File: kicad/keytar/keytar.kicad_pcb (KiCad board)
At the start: 2 copper layers, 9 parts, among them J1 DIN-5_180degree, J2 USB_B, J3 Conn_01x02, U1 Pico

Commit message: properly implement PCB
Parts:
- added  : MountingHole_3.2mm_M3, MountingHole:MountingHole_3.2mm_M3, F.Cu at (59.0, -7.02)
- added  : MountingHole_3.2mm_M3, MountingHole:MountingHole_3.2mm_M3, F.Cu at (19.2, -58.0)
- added J4: Conn_01x04, Connector_PinHeader_2.54mm:PinHeader_1x04_P2.54mm_Horizontal, F.Cu at (21.4, -38.6)
- J1: value DIN-5_180degree -> (none)
- R1, R2, R3: footprint Resistor_THT:R_Axial_DIN0411_L9.9mm_D3.6mm_P5.08mm_Vertical -> Resistor_THT:R_Axial_DIN0411_L9.9mm_D3.6mm_P12.70mm_Horizontal
- moved J3 189.7 mm to (8.94, -38.6), turned to 270 degrees
- moved R3 187.2 mm to (4.75, -47.9), turned to 0 degrees
- moved R1 159.7 mm to (52.7, -70.1), turned to 270 degrees
- moved U1 157.6 mm to (38.0, -46.2)
- moved RV1 144.8 mm to (52.5, -76.5), turned to 0 degrees
- moved RV2 144.4 mm to (8.51, -76.5), turned to 0 degrees
- moved J1 140.6 mm to (64.4, -61.0), turned to 90 degrees
- moved R2 134.0 mm to (52.7, -53.4), turned to 270 degrees
- moved J2 100.1 mm to (60.9, -42.6), turned to 0 degrees
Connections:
- J1 pad 2: Net-(J1-Pad2) -> GND
- U1 pad 3: Net-(J1-Pad2) -> GND
- U1 pad 38: GND -> Net-(U1-Pad38)
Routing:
- net Net-(J3-Pad2): track 20.4 -> 126.8 mm
- net Net-(J4-Pad2): track 0.00 -> 63.9 mm
- net Net-(RV2-Pad2): track 0.00 -> 58.6 mm
- net GND: track 0.00 -> 53.2 mm
- net Net-(R2-Pad2): track 0.00 -> 43.3 mm
- net Net-(J2-Pad1): track 0.00 -> 33.5 mm
- net Net-(RV1-Pad2): track 0.00 -> 33.0 mm
- net Net-(J3-Pad1): track 20.3 -> 46.3 mm
- net Net-(J4-Pad4): track 0.00 -> 17.9 mm
- net Net-(R3-Pad1): track 100.1 -> 114.9 mm
- net Net-(J4-Pad3): track 0.00 -> 14.3 mm
- net Net-(J2-Pad5): track 0.00 -> 12.0 mm
- net Net-(J4-Pad1): track 0.00 -> 8.33 mm
- net Net-(J1-Pad5): track 9.78 -> 7.25 mm
- net Net-(J1-Pad4): track 9.78 -> 7.93 mm
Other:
- board outline added: 76 x 95 mm
- board text added: "Garbage Keytar v0.1 designed by AberDerBart"

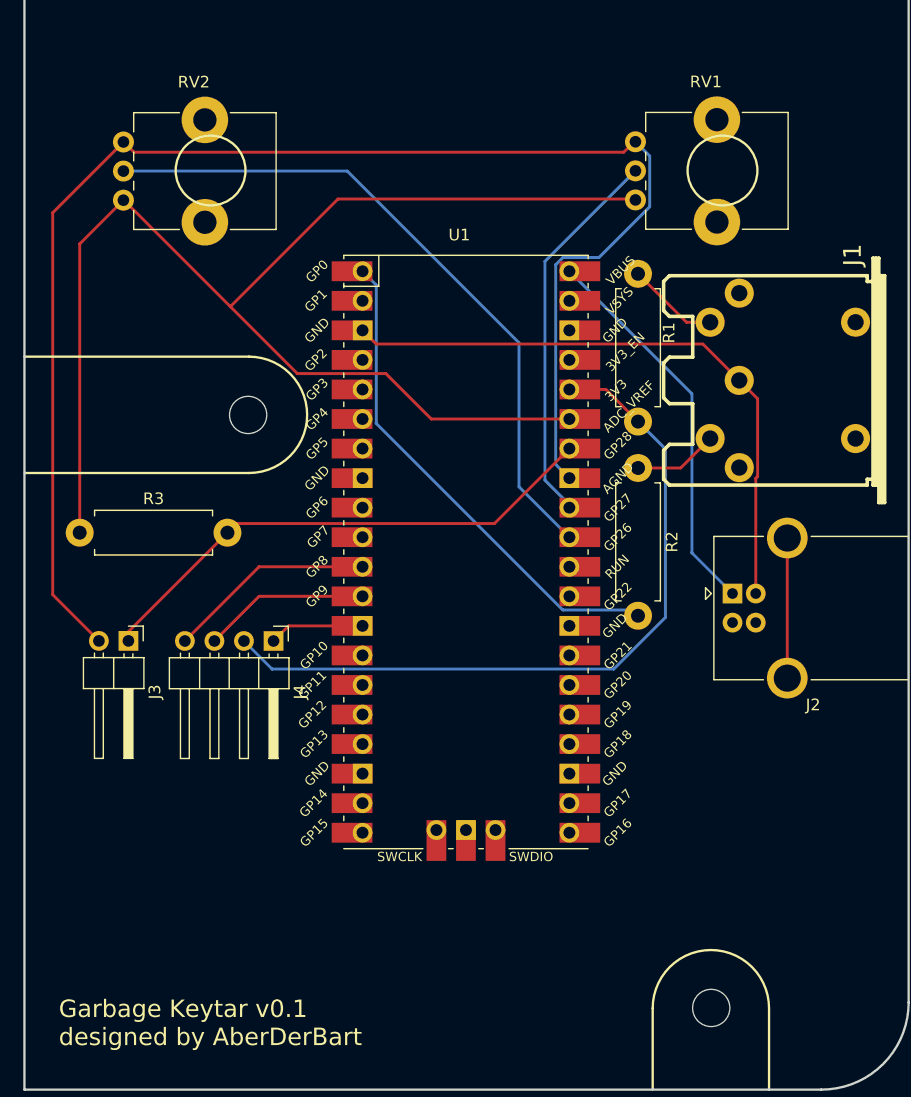
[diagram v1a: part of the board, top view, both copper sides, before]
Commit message: add power via MIDI to pcb
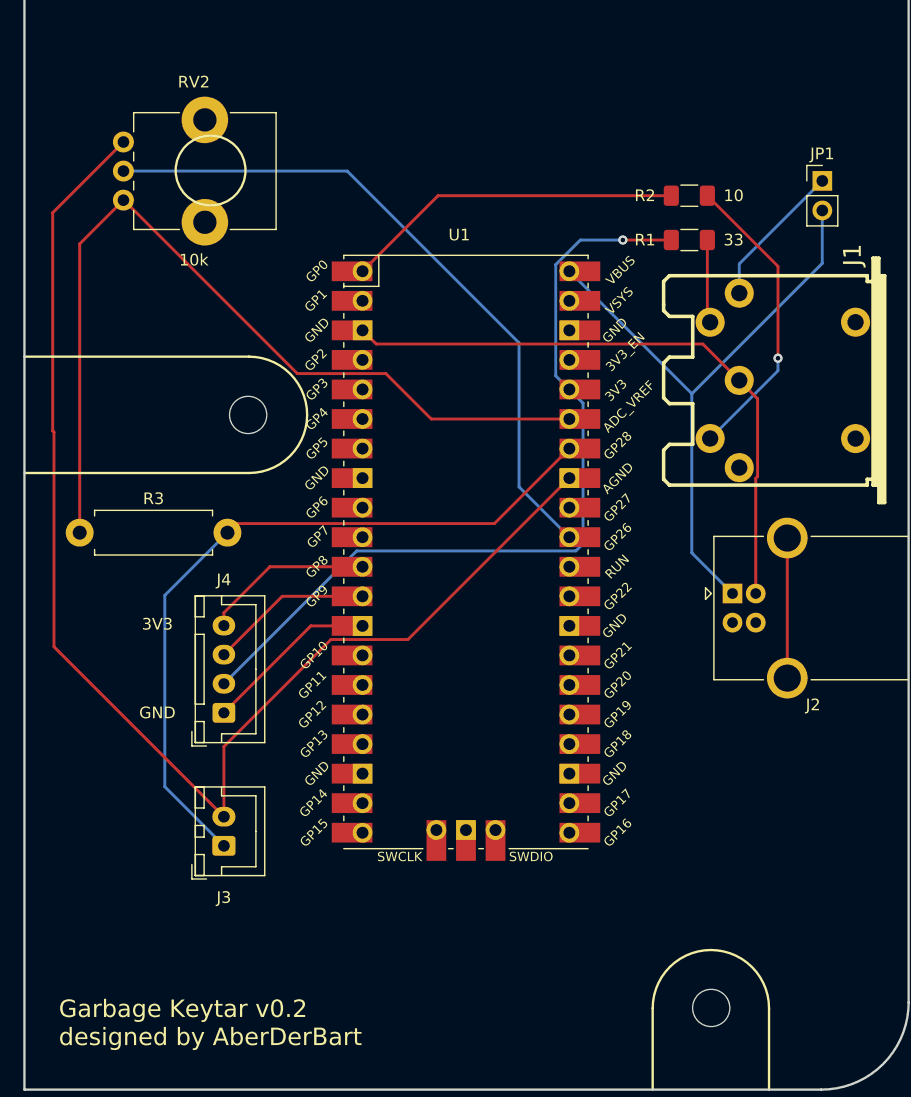
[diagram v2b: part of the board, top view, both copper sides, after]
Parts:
- removed RV1: R_POT, Potentiometer_THT:Potentiometer_Alps_RK09K_Single_Vertical
- added JP1: Jumper, Connector_PinHeader_2.54mm:PinHeader_1x02_P2.54mm_Vertical, F.Cu at (68.6, -78.1)
- J3: footprint Connector_PinHeader_2.54mm:PinHeader_1x02_P2.54mm_Horizontal -> Connector_JST:JST_XH_B2B-XH-A_1x02_P2.50mm_Vertical
- J4: footprint Connector_PinHeader_2.54mm:PinHeader_1x04_P2.54mm_Horizontal -> Connector_JST:JST_XH_B4B-XH-A_1x04_P2.50mm_Vertical
- R1, R2: footprint Resistor_THT:R_Axial_DIN0411_L9.9mm_D3.6mm_P12.70mm_Horizontal -> Resistor_SMD:R_1206_3216Metric_Pad1.30x1.75mm_HandSolder
- RV2: value R_POT -> 10k
- moved R2 23.8 mm to (57.1, -76.8), turned to 180 degrees
- moved J3 19.4 mm to (17.1, -21.0), turned to 90 degrees
- moved J4 7.50 mm to (17.1, -32.4), turned to 90 degrees
- moved R1 5.28 mm to (57.1, -73.0), turned to 180 degrees
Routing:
- net Net-(R3-Pad1): track 114.9 -> 76.3 mm
- net Net-(U1-Pad32): track 33.0 -> 0.25 mm
- net Net-(J2-Pad1): track 33.5 -> 53.9 mm
- net Net-(J1-Pad5): track 7.25 -> 25.8 mm, vias 0 -> 1
- net Net-(J3-Pad1): track 46.3 -> 64.7 mm
- net Net-(J3-Pad2): track 126.8 -> 111.9 mm
- net Net-(R2-Pad2): track 43.3 -> 29.2 mm
- net Net-(J1-Pad1): track 0.00 -> 12.6 mm
- net Net-(J4-Pad2): track 63.9 -> 71.6 mm, vias 0 -> 1
- net Net-(J4-Pad1): track 8.33 -> 15.0 mm
- net Net-(J4-Pad4): track 17.9 -> 14.7 mm
- net Net-(J1-Pad4): track 7.93 -> 7.17 mm
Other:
- board text added: "3V3"
- board text added: "GND"
- board text added: "Garbage Keytar v0.2 designed by AberDerBart"
- board text removed: "Garbage Keytar v0.1 designed by AberDerBart"

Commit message: redesign pcb
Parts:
- removed  : MountingHole_3.2mm_M3, MountingHole:MountingHole_3.2mm_M3 (x2)
- removed J1: , Eurocad:MIDI_DIN5
- removed R3: R, Resistor_THT:R_Axial_DIN0411_L9.9mm_D3.6mm_P12.70mm_Horizontal
- removed RV2: 10k, Potentiometer_THT:Potentiometer_Alps_RK09K_Single_Vertical
- removed U1: Pico, MCU_RaspberryPi_and_Boards:RPi_Pico_SMD_TH
- added J5: USB_A, Connector_USB:USB_A_Molex_67643_Horizontal, F.Cu at (106.6, 97.1)
- added JP2: USB Power, Connector_PinHeader_2.54mm:PinHeader_1x02_P2.54mm_Vertical, F.Cu at (130.8, 74.2)
- added RV1: R_POT, Connector_JST:JST_XH_B3B-XH-A_1x03_P2.50mm_Vertical, F.Cu at (115.4, 75.2)
- J3: value Conn_01x02 -> AudioJack2; footprint Connector_JST:JST_XH_B2B-XH-A_1x02_P2.50mm_Vertical -> Connector_Audio:Jack_6.35mm_Neutrik_NRJ4HF_Horizontal
- JP1: value Jumper -> MIDI Power
- moved J2 193.4 mm to (172.4, 115.3)
- moved J3 187.0 mm to (169.3, 87.6), turned to 0 degrees
- moved JP1 162.8 mm to (126.2, 74.2)
- moved R2 162.7 mm to (129.3, 69.0), turned to 0 degrees
- moved R1 156.4 mm to (129.3, 65.7), turned to 0 degrees
- moved J4 140.0 mm to (115.4, 67.4), turned to 0 degrees
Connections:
- net Net-(J4-Pad2) renamed +3V3
- J2 pad 1: Net-(J2-Pad1) -> Net-(J2-VBUS)
- J2 pad 2: Net-(J2-Pad2) -> unconnected-(J2-D--Pad2)
- J2 pad 3: Net-(J2-Pad3) -> unconnected-(J2-D+-Pad3)
- J2 pad 5: Net-(J2-Pad5) -> unconnected-(J2-Shield-Pad5)
- J4 pad 1: Net-(J4-Pad1) -> GND
- JP1 pad 2: Net-(J2-Pad1) -> +5V
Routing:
- net Net-(J3-Pad2): track 111.9 -> 0.00 mm
- net Net-(R3-Pad1): track 76.3 -> 0.00 mm
- net +3V3: track 71.6 -> 0.00 mm, vias 1 -> 0
- net Net-(J3-Pad1): track 64.7 -> 0.00 mm
- net Net-(RV2-Pad2): track 58.6 -> 0.00 mm
- net Net-(J2-Pad1): track 53.9 -> 0.00 mm
- net GND: track 53.2 -> 0.00 mm
- net Net-(U1-GPIO0): track 29.2 -> 0.00 mm
- net Net-(J1-Pad5): track 25.8 -> 0.00 mm, vias 1 -> 0
- net Net-(J4-Pad1): track 15.0 -> 0.00 mm
- net Net-(J4-Pin_4): track 14.7 -> 0.00 mm
- net Net-(J4-Pin_3): track 14.0 -> 0.00 mm
- net Net-(J1-Pad1): track 12.6 -> 0.00 mm
- net Net-(J2-Pad5): track 12.0 -> 0.00 mm
- net Net-(J1-Pad4): track 7.17 -> 0.00 mm
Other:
- board outline removed
- net class Default removed
- board text removed: "3V3"
- board text removed: "GND"
- board text removed: "Garbage Keytar v0.2 designed by AberDerBart"

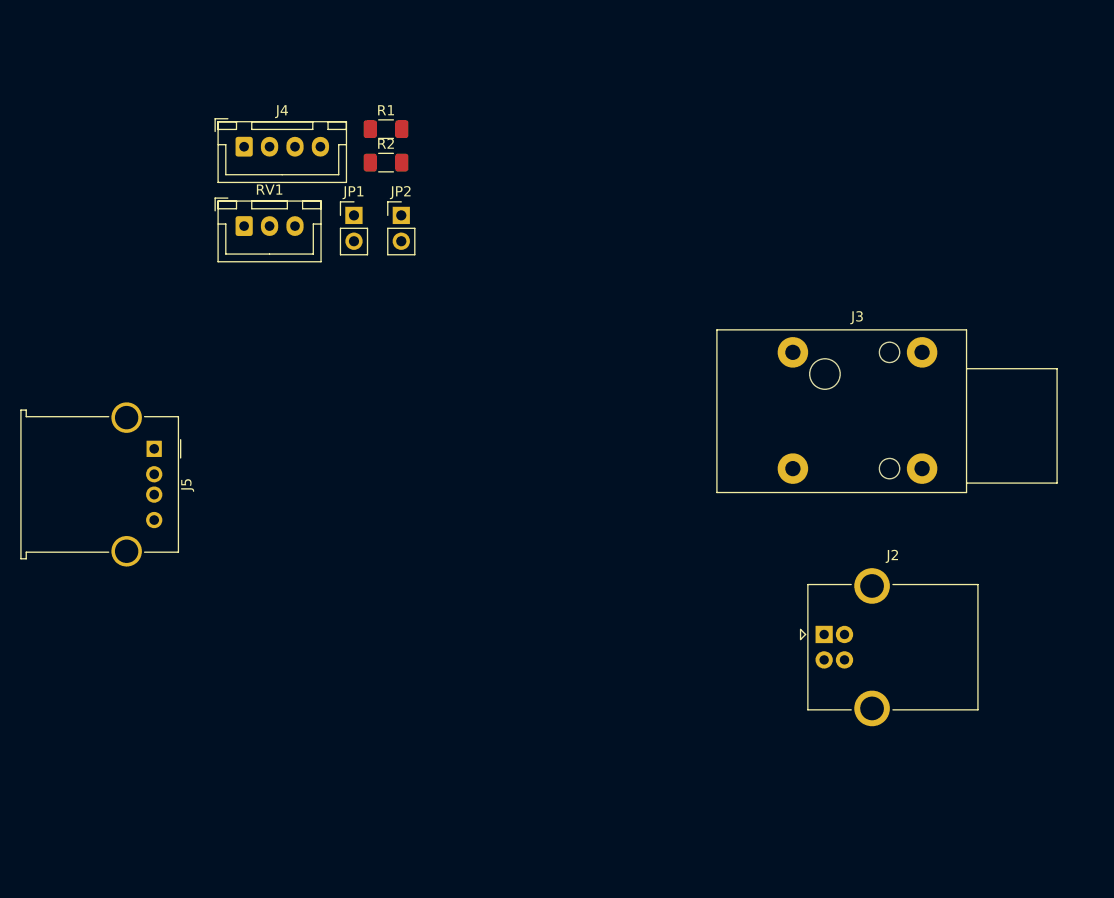
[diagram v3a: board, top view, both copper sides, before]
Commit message: shrink PCB, add USB and PS/2 ports
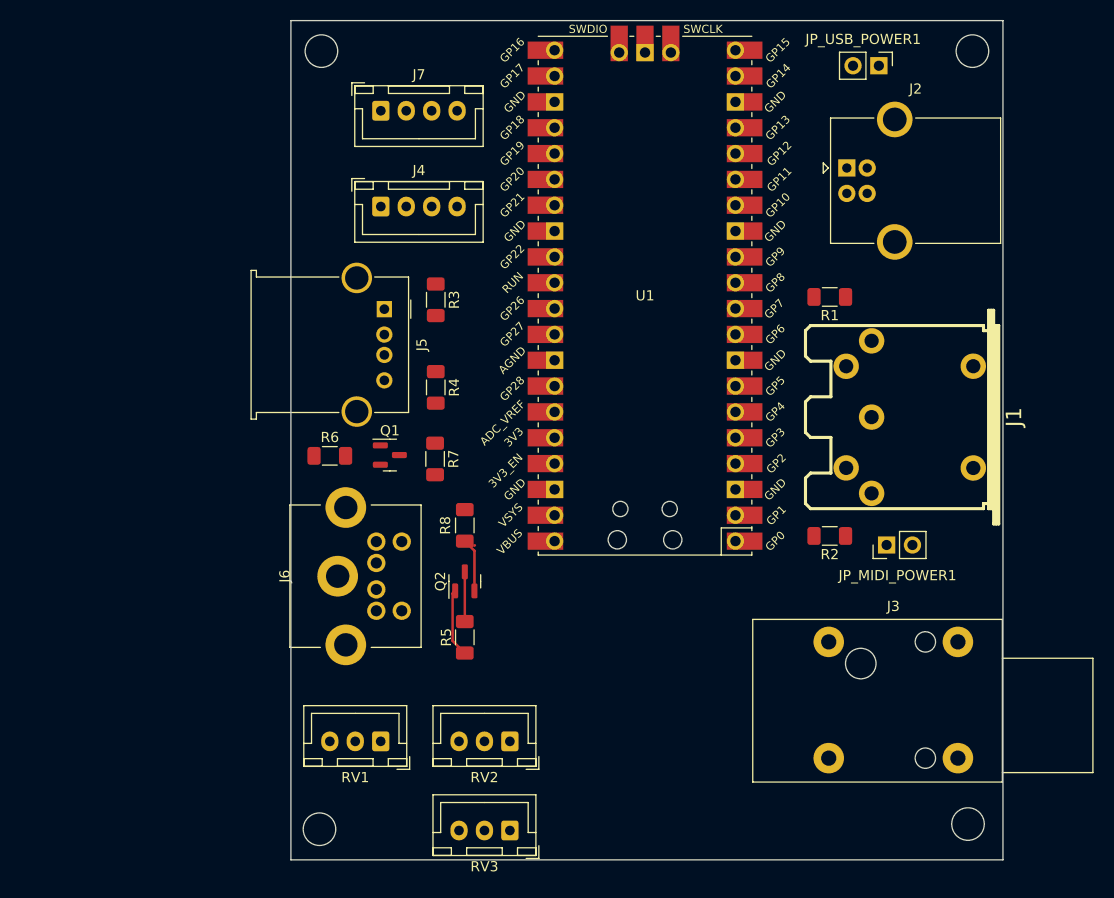
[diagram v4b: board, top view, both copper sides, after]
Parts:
- added J1: , Eurocad:MIDI_DIN5, F.Cu at (180.1, 94.0)
- added J6: Mini-DIN-6-Shielded, keyar-parts:EB-DIOS M06, F.Cu at (119.9, 109.6)
- added J7: Conn_01x04, Connector_JST:JST_XH_B4B-XH-A_1x04_P2.50mm_Vertical, F.Cu at (128.8, 63.9)
- added Q1: BSS138, Package_TO_SOT_SMD:SOT-23, F.Cu at (129.7, 97.7)
- added Q2: BSS138, Package_TO_SOT_SMD:SOT-23, F.Cu at (137.1, 110.1)
- added R3: 22, Resistor_SMD:R_1206_3216Metric_Pad1.30x1.75mm_HandSolder, F.Cu at (134.2, 82.4)
- added R4: 22, Resistor_SMD:R_1206_3216Metric_Pad1.30x1.75mm_HandSolder, F.Cu at (134.2, 91.1)
- added R5: 2k2, Resistor_SMD:R_1206_3216Metric_Pad1.30x1.75mm_HandSolder, F.Cu at (137.1, 115.6)
- added R6: 2k2, Resistor_SMD:R_1206_3216Metric_Pad1.30x1.75mm_HandSolder, F.Cu at (123.8, 97.8)
- added R7: 10k, Resistor_SMD:R_1206_3216Metric_Pad1.30x1.75mm_HandSolder, F.Cu at (134.2, 98.1)
- added R8: 10k, Resistor_SMD:R_1206_3216Metric_Pad1.30x1.75mm_HandSolder, F.Cu at (137.1, 104.6)
- added REF**: MountingHole_3.2mm_M3, MountingHole:MountingHole_3.2mm_M3, F.Cu at (122.8, 134.5)
- added REF**: MountingHole_3.2mm_M3, MountingHole:MountingHole_3.2mm_M3, F.Cu at (186.6, 134.0)
- added REF**: MountingHole_3.2mm_M3, MountingHole:MountingHole_3.2mm_M3, F.Cu at (123.0, 58.0)
- added REF**: MountingHole_3.2mm_M3, MountingHole:MountingHole_3.2mm_M3, F.Cu at (187.0, 58.0)
- added RV2: R_POT, Connector_JST:JST_XH_B3B-XH-A_1x03_P2.50mm_Vertical, F.Cu at (141.5, 125.9)
- added RV3: R_POT, Connector_JST:JST_XH_B3B-XH-A_1x03_P2.50mm_Vertical, F.Cu at (141.5, 134.6)
- added U1: Pico, MCU_RaspberryPi_and_Boards:RPi_Pico_SMD_TH, F.Cu at (154.8, 82.0)
- moved JP_MIDI_POWER1 61.6 mm to (178.6, 106.6), turned to 90 degrees
- moved R2 57.0 mm to (173.0, 105.7), turned to 180 degrees
- moved RV1 52.4 mm to (128.8, 125.9), turned to 180 degrees
- moved JP_USB_POWER1 49.2 mm to (177.8, 59.4), turned to -90 degrees
- moved R1 46.6 mm to (173.0, 82.2), turned to 180 degrees
- moved J2 45.9 mm to (174.7, 69.5)
- moved J3 28.7 mm to (172.9, 116.1)
- moved J5 26.5 mm to (129.2, 83.4)
- moved J4 14.7 mm to (128.8, 73.3)
- renumbered JP1 to JP_MIDI_POWER1, JP2 to JP_USB_POWER1
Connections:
- J5 pad 1: unconnected-(J5-VBUS-Pad1) -> +5V
- J5 pad 2: unconnected-(J5-D--Pad2) -> Net-(J5-D-)
- J5 pad 3: unconnected-(J5-D+-Pad3) -> Net-(J5-D+)
- J5 pad 4: unconnected-(J5-GND-Pad4) -> GND
- J5 pad 5: unconnected-(J5-Shield-Pad5) -> GND
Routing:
- net +5V: track 0.00 -> 6.71 mm
- net PS/2 CLK: track 0.00 -> 5.35 mm
- net Net-(Q2-D): track 0.00 -> 4.89 mm
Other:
- board outline added: 70 x 82.5 mm

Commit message: add battery management
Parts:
- added C1: 4u7, Capacitor_SMD:C_1206_3216Metric_Pad1.33x1.80mm_HandSolder, F.Cu at (148.3, 117.3)
- added C2: 4u7, Capacitor_SMD:C_1206_3216Metric_Pad1.33x1.80mm_HandSolder, F.Cu at (153.0, 117.3)
- added R9: 2k, Resistor_SMD:R_1206_3216Metric_Pad1.30x1.75mm_HandSolder, F.Cu at (143.7, 117.3)
- added U2: MCP73831-2-OT, Package_TO_SOT_SMD:SOT-23-5, F.Cu at (144.6, 111.1)
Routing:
- net +5V: track 6.71 -> 16.5 mm
- net Net-(U2-PROG): track 0.00 -> 6.32 mm
- net Net-(J8-Pin_1): track 0.00 -> 4.67 mm

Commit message: adjust midi pin
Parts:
- added BATT1: Conn_01x02, Connector_JST:JST_XH_B2B-XH-A_1x02_P2.50mm_Vertical, F.Cu at (155.2, 125.8)
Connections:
- R2 pad 2: Net-(U1-GPIO0) -> MIDI TX
- R3 pad 1: Net-(U1-GPIO2) -> Net-(J5-D+)
- R3 pad 2: Net-(J5-D+) -> USB D+
- R4 pad 1: Net-(U1-GPIO3) -> Net-(J5-D-)
- R4 pad 2: Net-(J5-D-) -> USB D-
- U1 pad 1: Net-(U1-GPIO0) -> unconnected-(U1-GPIO0-Pad1)
- U1 pad 4: Net-(U1-GPIO2) -> USB D+
- U1 pad 5: Net-(U1-GPIO3) -> USB D-
- U1 pad 9: unconnected-(U1-GPIO6-Pad9) -> MIDI TX
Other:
- board text added: "+"
- board text added: "-"

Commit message: route board
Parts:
- removed JP_MIDI_POWER1: MIDI Power, Connector_PinHeader_2.54mm:PinHeader_1x02_P2.54mm_Vertical
- removed JP_USB_POWER1: USB Power, Connector_PinHeader_2.54mm:PinHeader_1x02_P2.54mm_Vertical
- added C3: 22u, Capacitor_SMD:C_1206_3216Metric_Pad1.33x1.80mm_HandSolder, F.Cu at (139.1, 140.5)
- added D1: D_Schottky, Diode_SMD:D_SMA, F.Cu at (145.8, 138.0)
- added D2: D_Schottky, Diode_SMD:D_SMA, F.Cu at (174.7, 81.7)
- added D3: D_Schottky, Diode_SMD:D_SMA, F.Cu at (174.7, 59.0)
- added L1: 22u, Inductor_SMD:L_Bourns-SRN4018, F.Cu at (150.3, 133.7)
- added R10: 1k, Resistor_SMD:R_1206_3216Metric_Pad1.30x1.75mm_HandSolder, F.Cu at (139.2, 132.8)
- added R11: 7k5, Resistor_SMD:R_1206_3216Metric_Pad1.30x1.75mm_HandSolder, F.Cu at (139.2, 136.7)
- added U3: MT3608, Package_TO_SOT_SMD:SOT-23-6, F.Cu at (145.0, 133.7)
- C1: value 4u7 -> 22u
- C2: value 4u7 -> 10u
- U2: value MCP73831-2-OT -> ~; footprint Package_TO_SOT_SMD:SOT-23-5 -> Package_SO:HSOP-8-1EP_3.9x4.9mm_P1.27mm_EP2.3x2.3mm
- moved J7 64.2 mm to (131.5, 128.0), turned to 180 degrees
- moved R5 52.7 mm to (122.9, 64.8), turned to 0 degrees
- moved Q2 46.1 mm to (128.4, 64.8), turned to 0 degrees
- moved J4 45.4 mm to (131.5, 118.6), turned to 180 degrees
- moved R8 39.9 mm to (133.9, 64.8), turned to 180 degrees
- moved J6 33.5 mm to (120.0, 76.1)
- moved U2 29.5 mm to (163.1, 134.1), turned to 0 degrees
- moved C1 28.8 mm to (172.4, 133.0), turned to 180 degrees
- moved R1 27.4 mm to (172.4, 109.5)
- moved RV3 24.8 mm to (160.5, 118.5), turned to -90 degrees
- moved BATT1 23.5 mm to (174.0, 140.0)
- moved C2 23.5 mm to (160.5, 139.5), turned to 0 degrees
- moved R3 23.0 mm to (134.6, 105.5)
- moved R9 19.8 mm to (157.5, 131.5), turned to 90 degrees
- moved RV1 16.8 mm to (144.0, 118.5), turned to -90 degrees
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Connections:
- BATT1 pad 1: Net-(BATT1-Pin_1) -> +BATT
- C1 pad 1: Net-(BATT1-Pin_1) -> +BATT
- C2 pad 1: +5V -> VBUS
- J3 pad S: Net-(U1-GPIO22) -> GND
- J3 pad T: GND -> PEDAL
- RV1 pad 1: Net-(U1-AGND) -> GND
- RV1 pad 3: Net-(U1-ADC_VREF) -> +3V3
- RV2 pad 1: Net-(U1-AGND) -> GND
- RV2 pad 3: Net-(U1-ADC_VREF) -> +3V3
- RV3 pad 1: Net-(U1-AGND) -> GND
- RV3 pad 3: Net-(U1-ADC_VREF) -> +3V3
- U1 pad 29: Net-(U1-GPIO22) -> unconnected-(U1-GPIO22-Pad29)
- U1 pad 33: Net-(U1-AGND) -> unconnected-(U1-AGND-Pad33)
- U1 pad 35: Net-(U1-ADC_VREF) -> unconnected-(U1-ADC_VREF-Pad35)
- U1 pad 6: unconnected-(U1-GPIO4-Pad6) -> PEDAL
- U2 pad 1: BAT STATUS -> GND
- U2 pad 2: GND -> Net-(U2-PROG)
- U2 pad 3: Net-(BATT1-Pin_1) -> GND
- U2 pad 4: +5V -> VBUS
- U2 pad 5: Net-(U2-PROG) -> +BATT
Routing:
- net +3V3: track 0.00 -> 127.3 mm, vias 0 -> 1
- net VBUS: track 0.00 -> 102.2 mm
- net Net-(J4-Pin_4): track 0.00 -> 99.0 mm
- net Net-(J4-Pin_3): track 0.00 -> 98.3 mm
- net +5V: track 16.5 -> 102.3 mm
- net Net-(U1-GPIO26_ADC0): track 0.00 -> 43.7 mm
- net PS/2 DATA: track 0.00 -> 43.6 mm
- net USB D+: track 0.00 -> 38.6 mm
- net Net-(U1-GPIO27_ADC1): track 0.00 -> 37.8 mm
- net USB D-: track 0.00 -> 34.1 mm
- net Net-(U1-GPIO28_ADC2): track 0.00 -> 32.6 mm
- net PEDAL: track 0.00 -> 27.8 mm
- net Net-(J1-Pad4): track 0.00 -> 24.2 mm
- net MIDI TX: track 0.00 -> 22.0 mm
- net Net-(Q1-D): track 0.00 -> 19.1 mm
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- added copper zone on B.Cu, net GND
- added copper zone on F.Cu, net GND
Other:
- board size 70 x 82.5 mm -> 70 x 90 mm
